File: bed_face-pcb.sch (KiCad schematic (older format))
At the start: 106 parts, among them SW1 SW_Push, U1 ProMicro

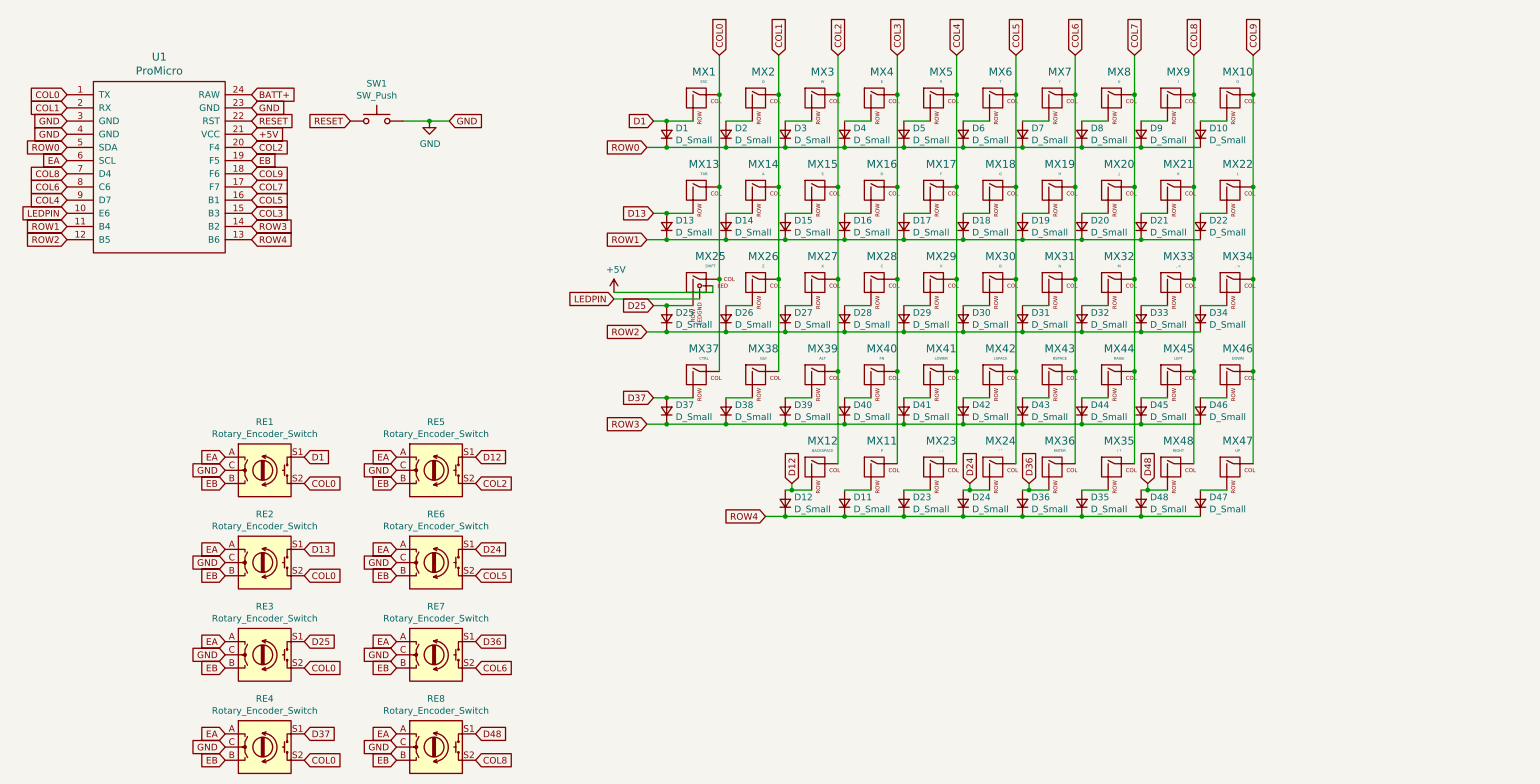
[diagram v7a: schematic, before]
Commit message: added encoder spots, mounting holes, moved pro micro * standard mount holes interfered with pro micro * rewired after moving, changed some pins * fixed space footprint * began moving used footprints to bed-face-footprints
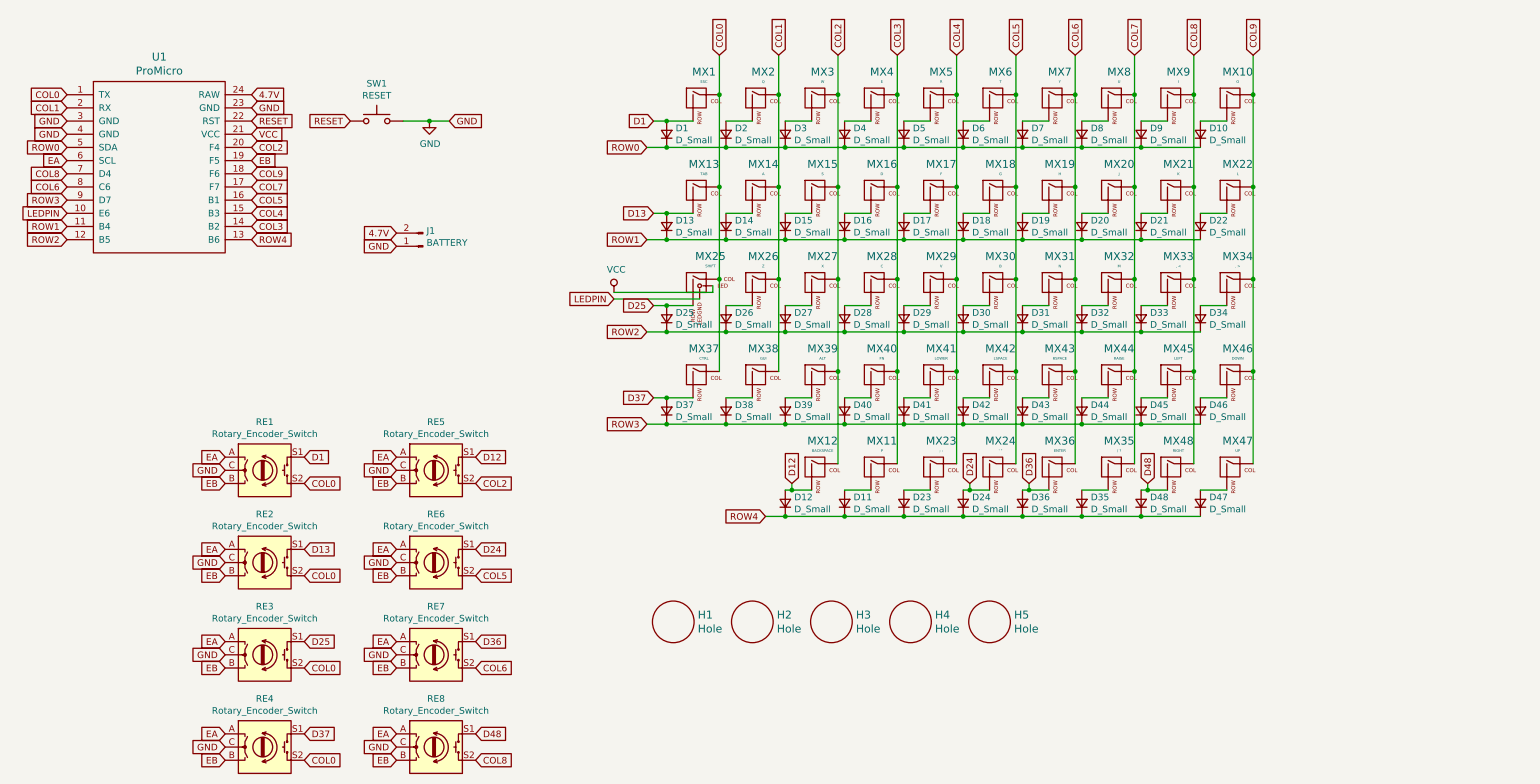
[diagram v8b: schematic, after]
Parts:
- added H1, H2, H3, H4, H5: Hole, bed-face-components:standoff_hole, symbol keebio:Hole
- added J1: BATTERY, Connector_JST:JST_PH_S2B-PH-K_1x02_P2.00mm_Horizontal, symbol Connector:Conn_01x02_Male
- MX1, MX10, MX11, MX12, MX13, MX14, MX15, MX16, MX17, MX18, MX19, MX2, MX20, MX21, MX22, MX23, MX24, MX26, MX27, MX28, MX29, MX3, MX30, MX31, MX32, MX33, MX34, MX35, MX36, MX37, MX38, MX39, MX4, MX40, MX41, MX44, MX45, MX46, MX47, MX48, MX5, MX6, MX7, MX8, MX9: footprint MX_Only:MXOnly-1U-NoLED-EDIT -> bed-face-components:MXOnly-1U-NoLED-EDIT
- MX25: footprint MX_Only:MXOnly-1U-EDIT -> bed-face-components:MXOnly-1U-EDIT
- MX42: footprint MX_Only:MXOnly-2U-ReversedStabilizers-NoLED-ComboSpace-EDIT -> bed-face-components:MXOnly-2U-ReversedStabilizers-NoLED-ComboSpace-EDIT
- MX43: footprint MX_Only:MXOnly-1U-NoLED-EDIT -> bed-face-components:MXOnly-1U-NoLED-EDIT-No-Corners
- SW1: value SW_Push -> RESET; footprint Keebio-Parts:SW_Tactile_SPST_Angled_MJTP1117 -> Keebio-Parts:SW_SPST_TL3342
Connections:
- net COL3: now also U1.14 (B2); no longer U1.15 (B3)
- net COL4: now also U1.15 (B3); no longer U1.9 (D7)
- net GND: now also J1.1 (Pin_1)
- net ROW3: now also U1.9 (D7); no longer U1.14 (B2)
- net +5V renamed VCC
- net BATT+ renamed 4.7V
- net 4.7V: now also J1.2 (Pin_2)
